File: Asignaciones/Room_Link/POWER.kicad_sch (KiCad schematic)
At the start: 0 parts

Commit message: ROOM-LINK update KICAD
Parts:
- added C7, C8: 0.1uF 25v, Capacitor_SMD:C_0805_2012Metric_Pad1.18x1.45mm_HandSolder, symbol Device:C
- added C9: 47uF 10, Capacitor_SMD:C_0805_2012Metric_Pad1.18x1.45mm_HandSolder, symbol Device:C_Polarized
- added D13, D16, D17, D18: LED, LED_SMD:LED_0805_2012Metric_Pad1.15x1.40mm_HandSolder, symbol Device:LED
- added F1: PTS120660V010, PTS12066V050:FUSC3216X68N, symbol nuevos simvolos:PTS120660V010
- added IC1: LM1117T-3.3, lm1117:TO254P470X1016X2222-3P, symbol LM1117T-3_3:LM1117T-3.3
- added PS1: HLK-PM12, KiCad:HLKPM12, symbol HLK-PM12:HLK-PM12
- added PS2: B0505S-W2R2, B0505S:B0505SW2R2, symbol B0505S-W2R2:B0505S-W2R2
- added R30: R, Resistor_SMD:R_0805_2012Metric_Pad1.20x1.40mm_HandSolder, symbol Device:R
- added R31: 2.2k, Resistor_SMD:R_0805_2012Metric_Pad1.20x1.40mm_HandSolder, symbol Device:R
- added R32: 470, Resistor_SMD:R_0805_2012Metric_Pad1.20x1.40mm_HandSolder, symbol Device:R
- added R33: 1k, Resistor_SMD:R_0805_2012Metric_Pad1.20x1.40mm_HandSolder, symbol Device:R
- added RV1: MOVTP20V275N, movtp:MOVTP20V275N, symbol MOVTP20V275N:MOVTP20V275N
- added Z1, Z2: 1SMA5918BT3G, huellas:DIOM5226X220N, symbol 1SMA5918BT3G:1SMA5918BT3G
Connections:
- net CON-DC+: now also R33.1
- net CON-L1: now also F1.1
- net CON-NEUT: now also PS1.1 (AC_1), RV1.2
- new net: F1.2, PS1.2 (AC_2), RV1.1
- new net: D16.2 (A), R31.2
- new net: D18.2 (A), R33.2
- new net: D17.2 (A), R32.2
- new net: D13.2 (A), R30.2
- new net +12V: C7.1, IC1.3 (IN), R31.1
- new net +3.3V: C8.1, C9.1, IC1.2 (OUT), PS2.2 (VIN), R32.1, Z1.2 (A)
- new net Earth: D13.1 (K), PS2.3 (0V), Z2.1 (K)
- new net GND: C7.2, C8.2, C9.2, D16.1 (K), D17.1 (K), D18.1 (K), IC1.1 (ADJ/GND), PS1.3 (-V0), PS1.4 (+V0), PS2.1 (GND), Z1.1 (K)
- new net VDD: PS2.4 (+VO), R30.1, Z2.2 (A)

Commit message: Added nuevos cambios
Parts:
- removed PS2: B0505S-W2R2, B0505S:B0505SW2R2, symbol B0505S-W2R2:B0505S-W2R2
- added U10: B0505XT-2WR2, nuevo simbolo:B0505S-W2R2, symbol 2023-07-29_00-48-08:B0505XT-2WR2
- F1: footprint PTS12066V050:FUSC3216X68N -> Fuse:Fuseholder_Cylinder-5x20mm_Stelvio-Kontek_PTF78_Horizontal_Open
- RV1: footprint movtp:MOVTP20V275N -> VAR_B72210S1140K501; symbol MOVTP20V275N:MOVTP20V275N -> B72210S1140K501:B72210S1140K501; MANUFACTURER (none) -> TDK; PARTREV (none) -> 2018-10; STANDARD (none) -> IPC-7351B
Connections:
- net +3.3V: now also U10.2 (VIN)
- net Earth: now also U10.4 (0V)
- net GND: now also U10.1 (GND)
- net VDD: now also U10.5 (+VO)
- no-connect marks 0 -> 1
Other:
- moved on the sheet: D13, R30, Z2

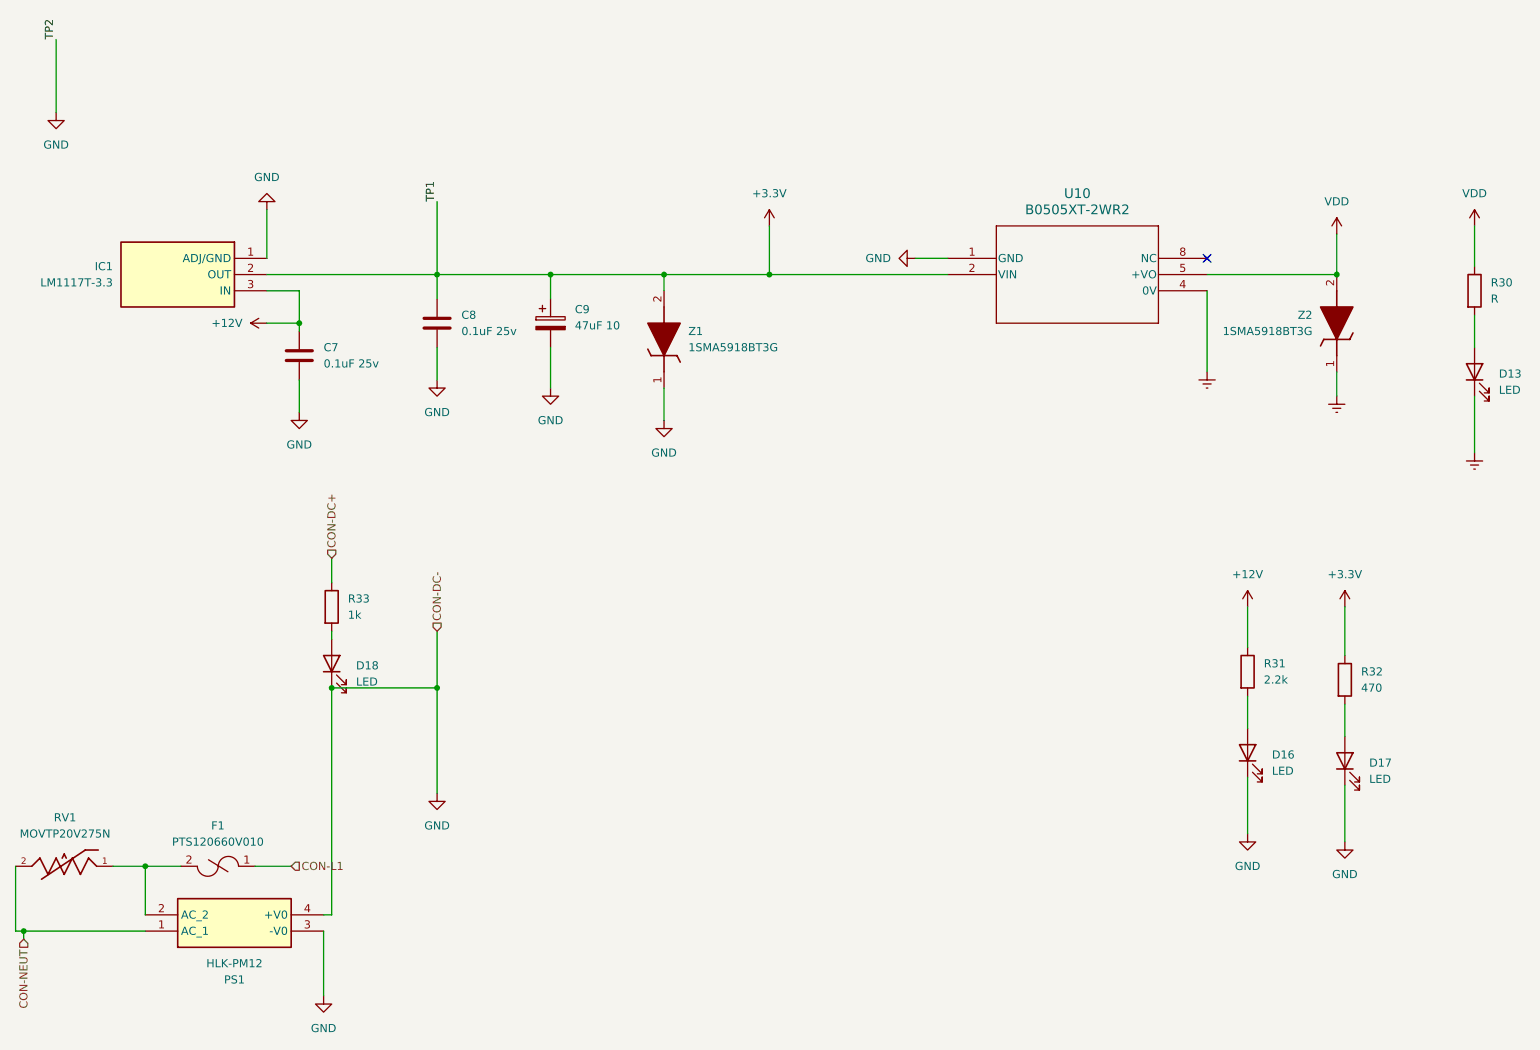
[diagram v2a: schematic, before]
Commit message: Place component Added & routing
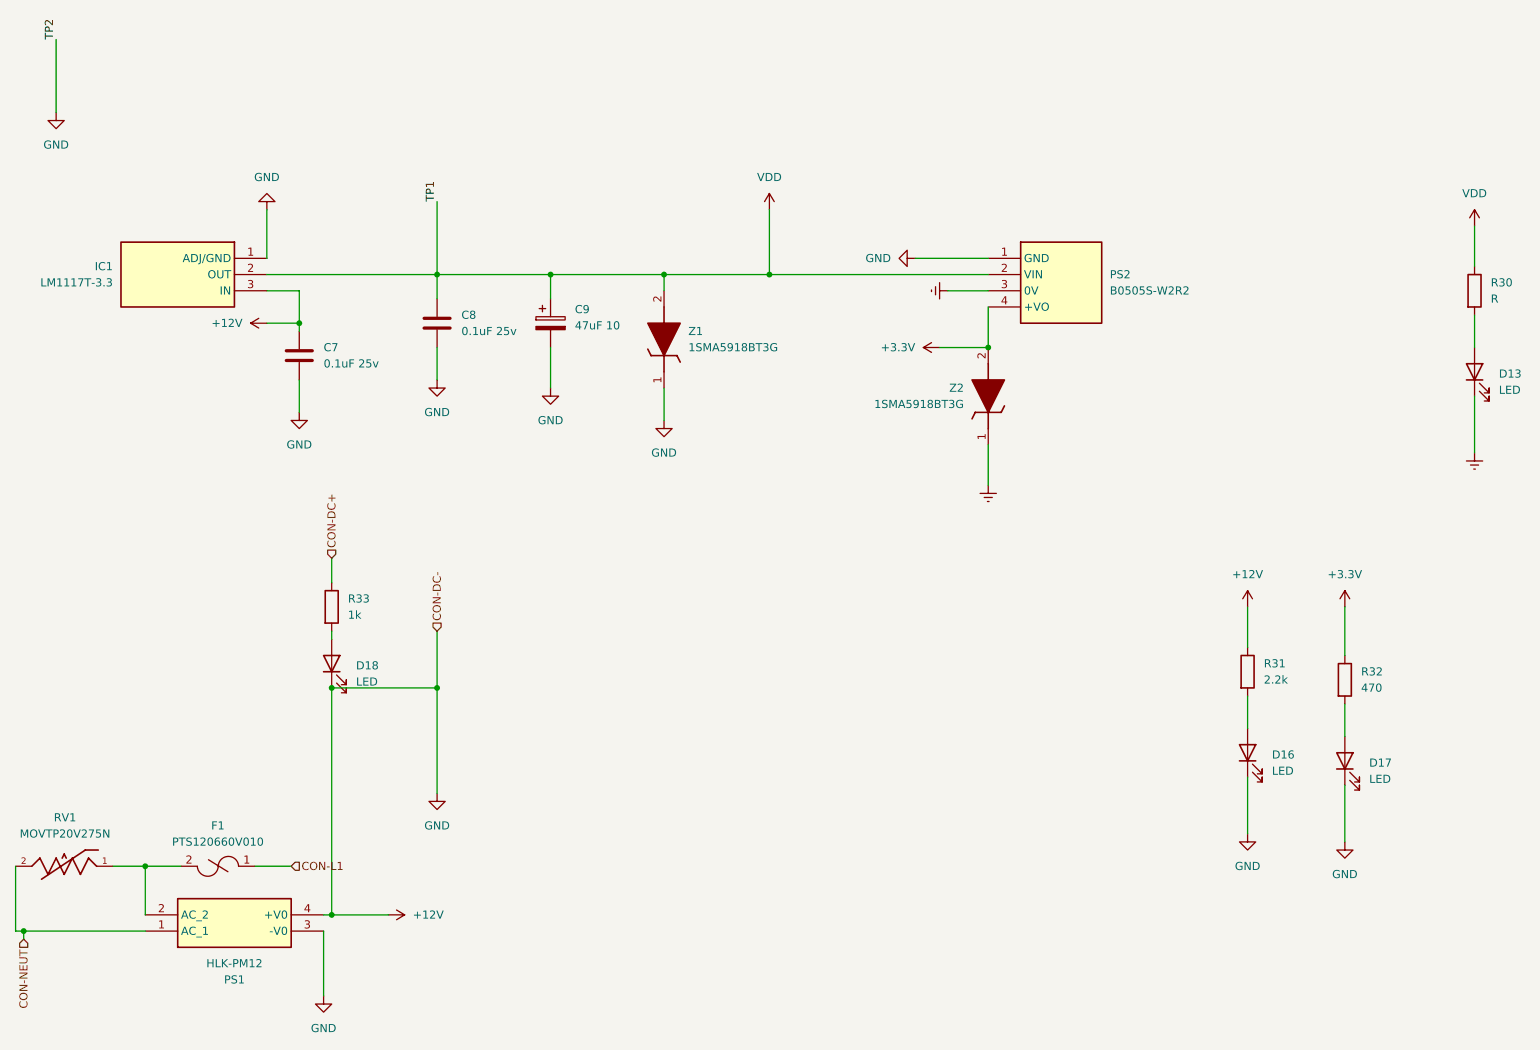
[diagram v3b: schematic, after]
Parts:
- removed U10: B0505XT-2WR2, nuevo simbolo:B0505S-W2R2, symbol 2023-07-29_00-48-08:B0505XT-2WR2
- added PS2: B0505S-W2R2, B0505SW2R2, symbol B0505S-W2R2:B0505S-W2R2
- C7, C8, C9: footprint Capacitor_SMD:C_0805_2012Metric_Pad1.18x1.45mm_HandSolder -> Capacitor_SMD:C_0805_2012Metric
- D13, D16, D17, D18: footprint LED_SMD:LED_0805_2012Metric_Pad1.15x1.40mm_HandSolder -> LED_SMD:LED_0805_2012Metric
- R30, R31, R32, R33: footprint Resistor_SMD:R_0805_2012Metric_Pad1.20x1.40mm_HandSolder -> Resistor_SMD:R_0805_2012Metric
- RV1: footprint VAR_B72210S1140K501 -> B722:B72210S1140K501
- Z1, Z2: footprint huellas:DIOM5226X220N -> Diode_SMD:D_SMB
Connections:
- net GND is gone; now on net +12V: C7.2, C8.2, C9.2, D16.1 (K), D17.1 (K), D18.1 (K), IC1.1 (ADJ/GND), PS1.3 (-V0), PS1.4 (+V0), Z1.1 (K)
- net +12V: now also PS2.1 (GND)
- net +3.3V: now also Z2.2 (A), PS2.4 (+VO); no longer C8.1, C9.1, IC1.2 (OUT), Z1.2 (A)
- net Earth: now also PS2.3 (0V)
- net VDD: now also C8.1, C9.1, IC1.2 (OUT), Z1.2 (A), PS2.2 (VIN); no longer Z2.2 (A)
- no-connect marks 1 -> 0
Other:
- moved on the sheet: Z2

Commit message: Terminado'disque'
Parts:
- PS2: footprint B0505SW2R2 -> B0505S:B0505SW2R2
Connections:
- net CON-DC+: no longer names the net of R33.1
